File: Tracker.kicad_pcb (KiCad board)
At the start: 4 copper layers, 100 x 70 mm, 278 parts, among them J1 Vehicle 12V 2X2, J2 Conn_Coaxial, J3 USB_C_Receptacle_USB2.0_16P, J4 Conn_01x05, J5 Micro_SD_Card_Det_Hirose_DM3AT, J6 SIM8060-6-1-14-00-A, J7 Conn_Coaxial, J8 Conn_Coaxial, Q1 CSD16406Q3, Q2 CSD16406Q3, Q3 2N7002, Q4 2N7002, Q5 DMT6007LFGQ-7, Q6 MMBT3904, Q7 MMBT3904, U1 TPS2121RUXR, U10 LM76003QRNPRQ1, U11 MAX-M10S, U12 LM74700, U13 TPS3840DL30DBVR, U14 USBLC6-2SC6, U15 TMP1075DGKR, U16 ATECC608B-SSHDA, U17 USBLC6-2SC6, U18 ASM330LHHTR, U19 TCA9535PWR, U2 TPS63802DLAR, U21 W25N01GVZEIG, U22 SN74AXC4T245QPWRQ1, U23 SN74AXC4T245QPWRQ1, U24 TPS22918TDBVTQ1, U25 SN74AXC4T245QPWRQ1_CELL, U26 SN74AXC4T245QPWRQ1, U27 BG95-M3, U3 TPS61094DSSR, U4 BQ29700DSER, U5 INA3221AIRGVR, U6 TPS3840DL35DBVR, U7 TPS62840DLCR, U8 TPS62840DLCR, U9 BQ25601DRTWR

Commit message: update
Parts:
- J8: moved to F.Cu
- moved CSC1 16.2 mm to (186.0, 126.5)
- moved L1 9.22 mm to (168.0, 131.5)
- moved Q4 7.15 mm to (124.3, 123.8)
- moved U25 5.20 mm to (176.5, 119.8)
- moved R46 4.10 mm to (112.5, 129.5)
- moved R47 4.10 mm to (114.8, 129.5)
- moved C51 4.10 mm to (108.0, 129.5)
- moved C57 4.10 mm to (110.3, 129.5)
- moved C60 4.10 mm to (126.6, 129.2)
- moved R45 4.10 mm to (117.1, 129.5)
- moved R48 4.10 mm to (121.4, 129.2)
- moved R49 4.10 mm to (119.3, 129.4)
- moved R61 4.10 mm to (124.9, 129.2)
- moved R62 4.10 mm to (123.1, 129.2)
- moved J2 3.50 mm to (102.2, 130.5)
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
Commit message: Rearrange PCB component placement
Relocate and rotate components across the board, adjust footprint text and pad orientations, and lock the battery holder footprint.
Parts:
- moved C37 229.1 mm to (183.5, 136.2)
- moved C39 227.5 mm to (183.5, 134.2)
- moved C7 209.0 mm to (161.5, 127.2)
- moved C1 208.9 mm to (161.5, 129.5)
- moved C5 207.1 mm to (178.5, 128.2)
- moved C12 205.8 mm to (161.5, 125.0)
- moved C17 205.7 mm to (149.2, 152.2), turned to 180 degrees
- moved C2 200.0 mm to (174.2, 119.5), turned to 90 degrees
- moved C10 196.5 mm to (165.8, 133.2), turned to 90 degrees
- moved C41 185.2 mm to (135.7, 134.0)
- moved R31 169.7 mm to (117.9, 108.5), turned to 180 degrees
- moved R55 169.6 mm to (105.5, 132.0), turned to 90 degrees
- moved R24 157.9 mm to (110.1, 101.7), turned to 90 degrees
- moved C33 157.4 mm to (117.0, 101.8), turned to 90 degrees
- moved C8 151.9 mm to (138.0, 102.9), turned to 90 degrees
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
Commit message: updt
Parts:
- moved TP1 11.2 mm to (47.7, 171.6)
- moved TP12 0.61 mm to (37.0, 178.2)
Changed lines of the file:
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@@
 	(footprint "TestPoint:TestPoint_Pad_D1.5mm"
 		(layer "F.Cu")
-		(at 37.1164 178.8028)
+		(at 37 178.2)
 		(descr "SMD pad as test Point, diameter 1.5mm")
 		(tags "test point SMD pad")
@@
 	(footprint "TestPoint:TestPoint_Pad_D1.5mm"
 		(layer "F.Cu")
-		(at 37.1164 175.2528)
+		(at 47.7 171.6)
 		(descr "SMD pad as test Point, diameter 1.5mm")
 		(tags "test point SMD pad")

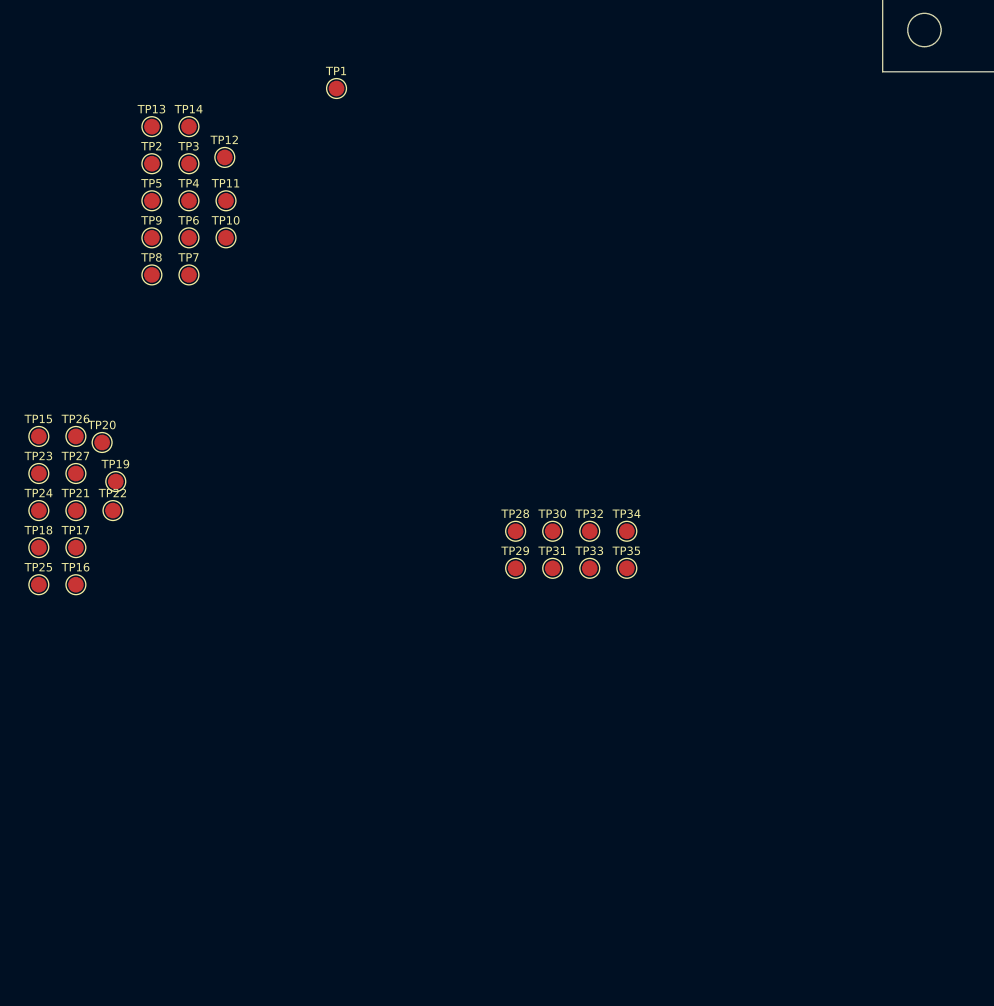
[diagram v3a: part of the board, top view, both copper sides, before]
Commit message: TP location update
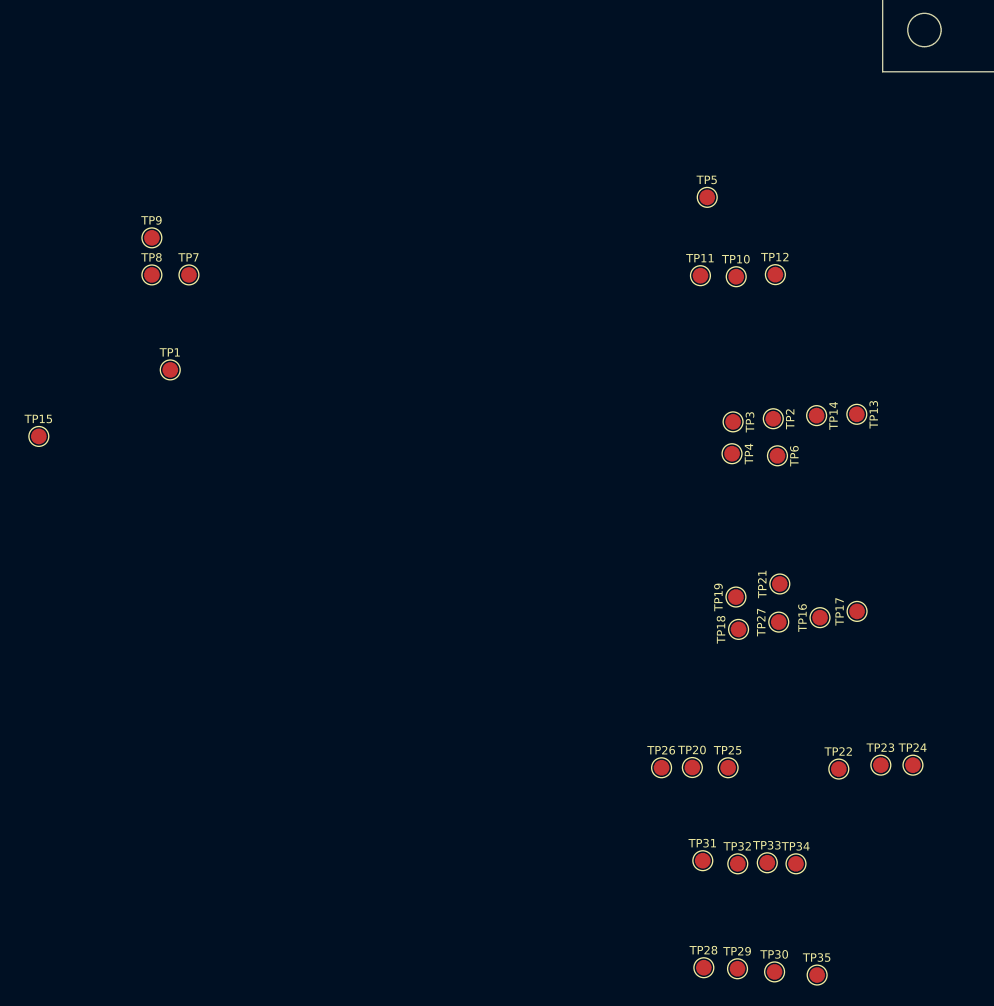
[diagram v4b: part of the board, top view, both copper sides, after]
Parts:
- moved TP24 87.2 mm to (102.9, 236.4)
- moved TP23 85.3 mm to (99.8, 236.4)
- moved TP17 75.1 mm to (97.5, 221.7), turned to 90 degrees
- moved TP22 73.8 mm to (95.8, 236.8)
- moved TP13 72.9 mm to (97.5, 202.8), turned to -90 degrees
- moved TP16 71.3 mm to (94.0, 222.3), turned to 90 degrees
- moved TP27 68.8 mm to (90.0, 222.7), turned to 90 degrees
- moved TP25 68.3 mm to (85.2, 236.7)
- moved TP21 67.8 mm to (90.2, 219.1), turned to 90 degrees
- moved TP18 67.5 mm to (86.2, 223.4), turned to 90 degrees
- moved TP14 66.2 mm to (93.7, 202.9), turned to -90 degrees
- moved TP20 64.5 mm to (81.8, 236.6)
- moved TP26 64.4 mm to (78.8, 236.7)
- moved TP2 64.3 mm to (89.5, 203.2), turned to -90 degrees
- moved TP19 60.4 mm to (86.0, 220.3), turned to 90 degrees
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
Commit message: Update Tracker.kicad_pcb
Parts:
- moved TP35 87.7 mm to (146.6, 186.6)
- moved TP30 86.5 mm to (142.1, 187.4)
- moved TP29 85.5 mm to (138.2, 188.1)
- moved TP28 85.0 mm to (134.9, 188.6)
- moved J8 72.0 mm to (160.9, 102.0), turned to 90 degrees
- moved J7 64.7 mm to (155.7, 102.0), turned to 90 degrees
- moved C91 12.7 mm to (161.5, 113.7), turned to 180 degrees
- moved C89 10.7 mm to (161.5, 112.2), turned to 180 degrees
- moved C86 8.76 mm to (161.5, 110.8), turned to 180 degrees
- moved R69 8.49 mm to (178.0, 161.0)
- moved C92 6.88 mm to (161.5, 109.5), turned to 180 degrees
- moved C83 5.08 mm to (161.5, 108.2), turned to 180 degrees
- moved J2 4.96 mm to (102.1, 137.4)
- moved C76 3.30 mm to (161.5, 106.8), turned to 180 degrees
- moved C78 1.89 mm to (161.5, 105.2), turned to 180 degrees
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
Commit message: Update Tracker.kicad_pcb
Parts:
- moved L7 23.7 mm to (105.2, 141.9)
- moved R38 22.0 mm to (105.2, 143.4)
- moved U11 19.1 mm to (112.9, 140.8)
- moved C38 19.1 mm to (113.4, 134.6)
- moved C41 19.1 mm to (116.6, 134.6)
- moved C42 19.1 mm to (110.9, 134.6)
- moved C45 18.9 mm to (105.2, 145.2)
- moved U16 13.6 mm to (123.1, 143.2)
- moved U21 13.6 mm to (126.4, 136.6)
- moved U15 13.6 mm to (133.6, 137.1)
- moved U18 13.6 mm to (131.1, 143.1)
- moved C54 11.8 mm to (135.3, 141.2)
- moved C55 11.8 mm to (135.3, 142.9)
- moved C58 11.8 mm to (135.2, 144.7)
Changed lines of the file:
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@@
 	(footprint "Capacitor_SMD:C_0402_1005Metric"
 		(layer "F.Cu")
-		(at 130 134)
+		(at 110.9 134.6375)
 		(descr "Capacitor SMD 0402 (1005 Metric), square (rectangular) end terminal, IPC-7351 nominal, (Body size source: IPC-SM-782 page 76, https://www.pcb-3d.com/wordpress/wp-content/uploads/ipc-sm-782a_amendment_1_and_2.pdf)")
 		(tags "capacitor")
@@
 	(footprint "Inductor_SMD:L_0402_1005Metric"
 		(layer "F.Cu")
-		(at 127.5 134)
+		(at 105.19 141.9)
 		(descr "Inductor SMD 0402 (1005 Metric), square (rectangular) end terminal, IPC-7351 nominal, (Body size source: http://www.tortai-tech.com/upload/download/2011102023233369053.pdf)")
 		(tags "inductor")
 		(property "Reference" "L7"
-			(at 0 -1.17 0)
+			(at -1.89 0.075 0)
 			(layer "F.SilkS")
 			(effects
@@
 	(footprint "Capacitor_SMD:C_0603_1608Metric"
 		(layer "F.Cu")
-		(at 135.725 134)
+		(at 116.625 134.6375)
 		(descr "Capacitor SMD 0603 (1608 Metric), square (rectangular) end terminal, IPC-7351 nominal, (Body size source: IPC-SM-782 page 76, https://www.pcb-3d.com/wordpress/wp-content/uploads/ipc-sm-782a_amendment_1_and_2.pdf)")
 		(tags "capacitor")
@@
 	(footprint "Package_SO:SOIC-8_3.9x4.9mm_P1.27mm"
 		(layer "F.Cu")
-		(at 109.5 143.6 180)
+		(at 123.075 143.21 180)
 		(descr "SOIC, 8 Pin (JEDEC MS-012AA, https://www.analog.com/media/en/package-pcb-resources/package/pkg_pdf/soic_narrow-r/r_8.pdf)")
 		(tags "SOIC SO")
@@
 	(footprint "RF_GPS:ublox_MAX"
 		(layer "F.Cu")
-		(at 132 140.5 180)
+		(at 112.875 140.8 180)
 		(descr "ublox MAX 6/7/8, (https://www.u-blox.com/sites/default/files/MAX-8-M8-FW3_HardwareIntegrationManual_%28UBX-15030059%29.pdf)")
 		(tags "GPS ublox MAX 6/7/8")
@@
 	(footprint "SamacSys_Parts:LSM6DS3USTR"
 		(layer "F.Cu")
-		(at 117.5 143.512)
+		(at 131.075 143.122)
 		(descr "LGA-14(2.5x3x0.86)")
 		(tags "Integrated Circuit")
@@
 	(footprint "SamacSys_Parts:SON127P800X600X80-9N-D"
 		(layer "F.Cu")
-		(at 112.8 137 180)
+		(at 126.375 136.61 180)
 		(descr "8-Pad WSON 8x6-mm (Package Code ZE)")
 		(tags "Integrated Circuit")
@@
 	(footprint "Capacitor_SMD:C_0402_1005Metric"
 		(layer "F.Cu")
-		(at 132.5 134)
+		(at 113.4 134.6375)
 		(descr "Capacitor SMD 0402 (1005 Metric), square (rectangular) end terminal, IPC-7351 nominal, (Body size source: IPC-SM-782 page 76, https://www.pcb-3d.com/wordpress/wp-content/uploads/ipc-sm-782a_amendment_1_and_2.pdf)")
 		(tags "capacitor")
@@
 	(footprint "Resistor_SMD:R_0402_1005Metric"
 		(layer "F.Cu")
-		(at 125.08 134.03)
+		(at 105.25 143.45)
 		(descr "Resistor SMD 0402 (1005 Metric), square (rectangular) end terminal, IPC-7351 nominal, (Body size source: IPC-SM-782 page 72, https://www.pcb-3d.com/wordpress/wp-content/uploads/ipc-sm-782a_amendment_1_and_2.pdf)")
 		(tags "resistor")
 		(property "Reference" "R38"
-			(at -2.18 -0.03 0)
+			(at -2.325 0.025 0)
 			(layer "F.SilkS")
 			(effects
@@
 	(footprint "Capacitor_SMD:C_0402_1005Metric"
 		(layer "F.Cu")
-		(at 123.48 145.5)
+		(at 135.238 144.722)
 		(descr "Capacitor SMD 0402 (1005 Metric), square (rectangular) end terminal, IPC-7351 nominal, (Body size source: IPC-SM-782 page 76, https://www.pcb-3d.com/wordpress/wp-content/uploads/ipc-sm-782a_amendment_1_and_2.pdf)")
 		(tags "capacitor")
@@
 	(footprint "Capacitor_SMD:C_0402_1005Metric"
 		(layer "F.Cu")
-		(at 123.5 142)
+		(at 135.258 141.222)
 		(descr "Capacitor SMD 0402 (1005 Metric), square (rectangular) end terminal, IPC-7351 nominal, (Body size source: IPC-SM-782 page 76, https://www.pcb-3d.com/wordpress/wp-content/uploads/ipc-sm-782a_amendment_1_and_2.pdf)")
 		(tags "capacitor")
@@
 	(footprint "Capacitor_SMD:C_0402_1005Metric"
 		(layer "F.Cu")
-		(at 123.5 143.7)
+		(at 135.258 142.922)
 		(descr "Capacitor SMD 0402 (1005 Metric), square (rectangular) end terminal, IPC-7351 nominal, (Body size source: IPC-SM-782 page 76, https://www.pcb-3d.com/wordpress/wp-content/uploads/ipc-sm-782a_amendment_1_and_2.pdf)")
 		(tags "capacitor")
@@
 	(footprint "Package_SO:VSSOP-8_3x3mm_P0.65mm"
 		(layer "F.Cu")
-		(at 120 137.5 90)
+		(at 133.575 137.11 90)
 		(descr "VSSOP, 8 Pin (https://www.jedec.org/standards-documents/docs/mo-187-f)")
 		(tags "VSSOP SO JEDEC-MO-187-AA Texas_DGK0008A")
 		(property "Reference" "U15"
-			(at -4.35 0.9 90)
+			(at -8.837 -2.787 180)
 			(layer "F.SilkS")
 			(effects
@@
 	(footprint "Capacitor_SMD:C_0402_1005Metric"
 		(layer "F.Cu")
-		(at 123.5 140.25)
+		(at 105.225 145.225)
 		(descr "Capacitor SMD 0402 (1005 Metric), square (rectangular) end terminal, IPC-7351 nominal, (Body size source: IPC-SM-782 page 76, https://www.pcb-3d.com/wordpress/wp-content/uploads/ipc-sm-782a_amendment_1_and_2.pdf)")
 		(tags "capacitor")
 		(property "Reference" "C45"
-			(at 0 -1.16 0)
+			(at -2.15 0.1 0)
 			(layer "F.SilkS")
 			(effects

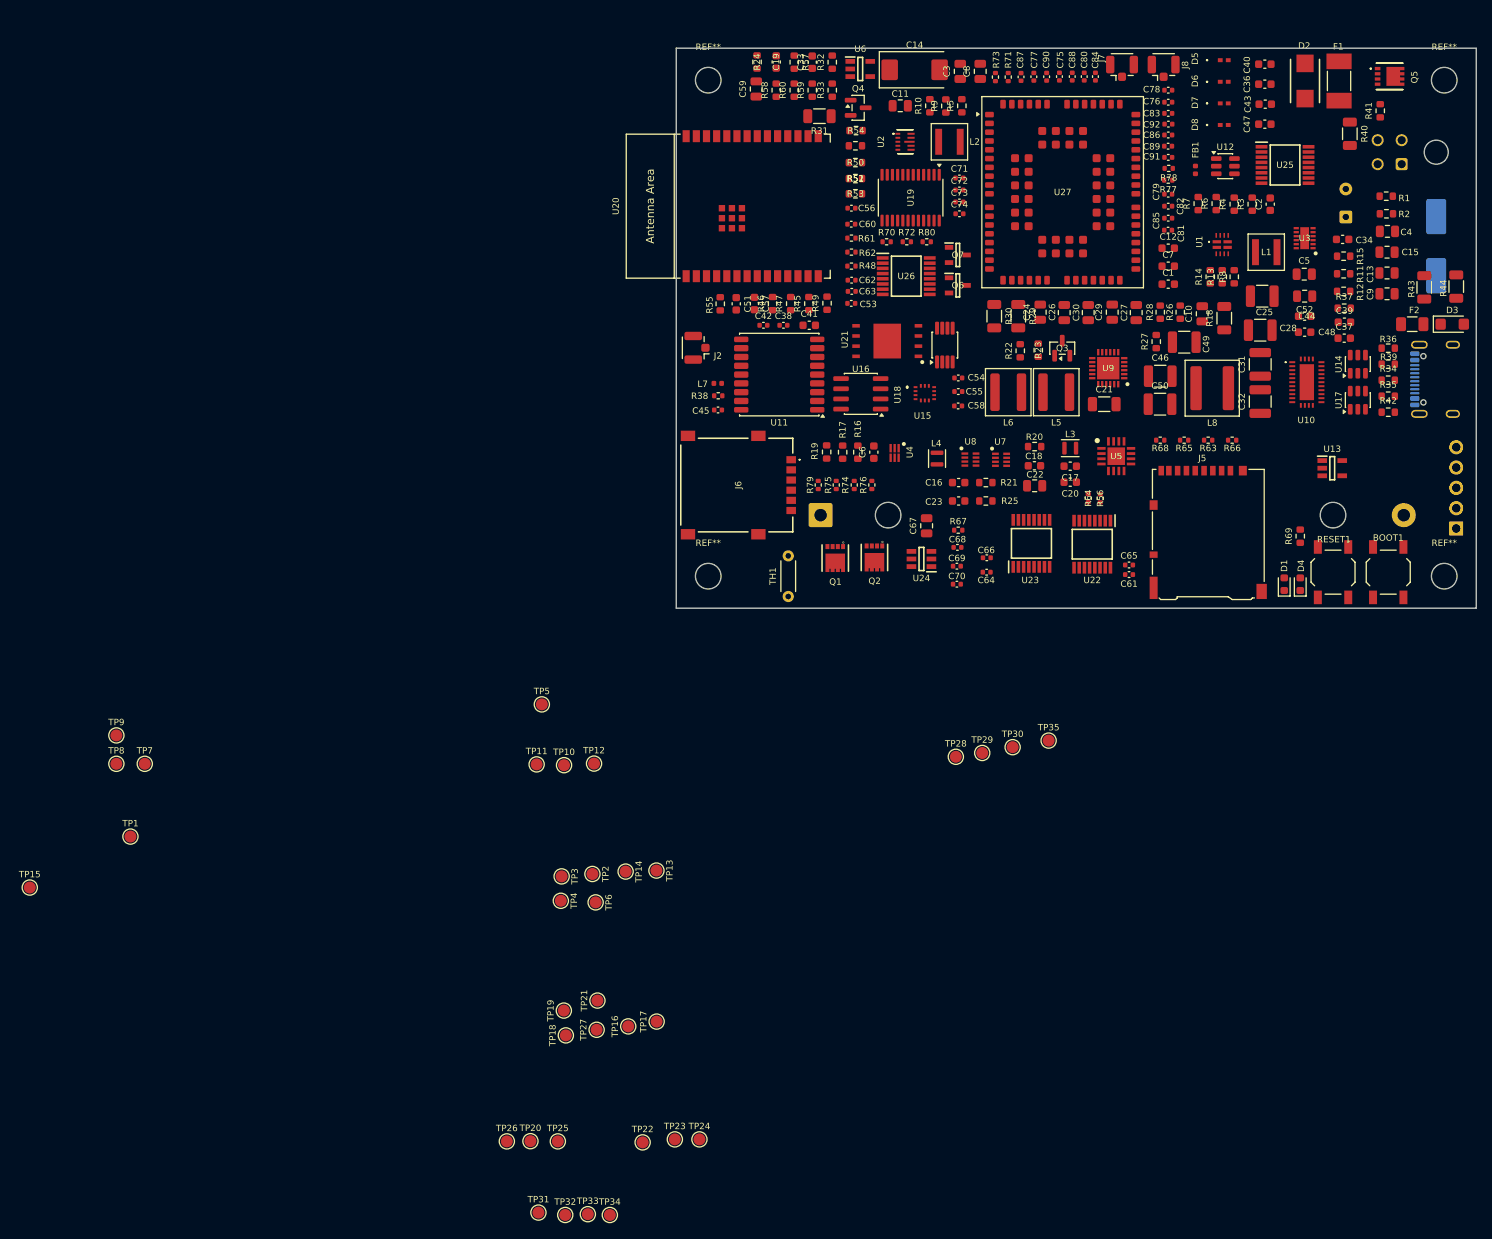
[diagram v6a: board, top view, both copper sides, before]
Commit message: relocation of TP
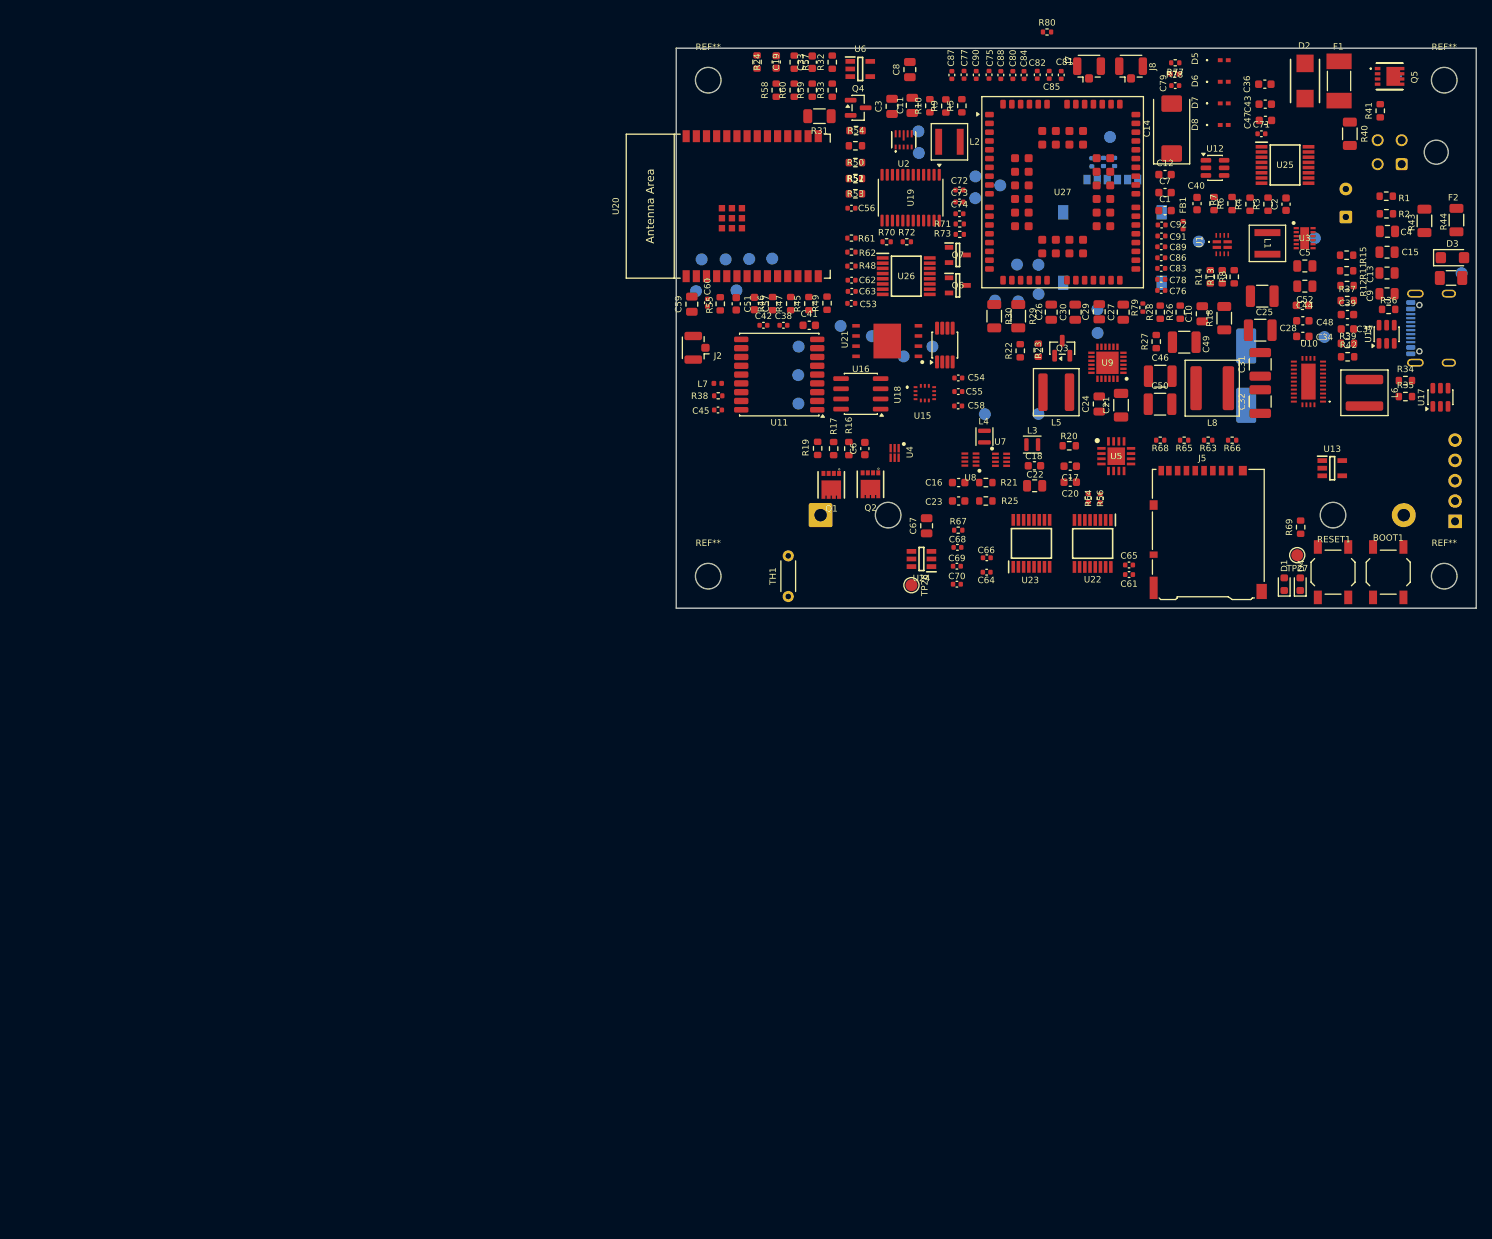
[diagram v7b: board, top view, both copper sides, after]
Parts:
- removed the J4 at (197.5, 160.0)
- J6, R74, R75, R76, TP1, TP10, TP11, TP12, TP13, TP14, TP15, TP16, TP17, TP18, TP19, TP2, TP20, TP21, TP22, TP23, TP24, TP25, TP28, TP29, TP3, TP30, TP31, TP32, TP33, TP34, TP35, TP4, TP5, TP6, TP7, TP8, TP9: moved to B.Cu
- moved TP15 194.8 mm to (198.2, 128.1), turned to 180 degrees
- moved TP34 148.5 mm to (154.2, 111.1), turned to 180 degrees
- moved TP31 140.6 mm to (137.4, 116.0), turned to -90 degrees
- moved TP32 139.7 mm to (140.5, 117.2), turned to 180 degrees
- moved TP33 135.9 mm to (137.4, 118.8), turned to 180 degrees
- moved TP13 135.6 mm to (189.9, 103.6)
- moved TP1 130.4 mm to (130.3, 113.1), turned to 180 degrees
- moved TP8 126.7 mm to (142.8, 131.7), turned to 180 degrees
- moved TP4 125.5 mm to (179.8, 123.8)
- moved TP9 122.5 mm to (139.8, 131.6), turned to 180 degrees
- moved TP7 113.7 mm to (138.6, 145.8), turned to 180 degrees
- moved TP20 113.6 mm to (109.1, 126.3), turned to -90 degrees
- moved TP14 110.0 mm to (181.0, 136.1)
- moved TP25 109.8 mm to (132.0, 137.3), turned to -90 degrees
- moved TP2 109.5 mm to (165.3, 124.2)
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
